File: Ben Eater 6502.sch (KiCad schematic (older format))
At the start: 8 parts, among them SW1 Reset, U1 W65C02SxP, U2 4011, U3 28C256, U4 4011, U5 W65C22SxP

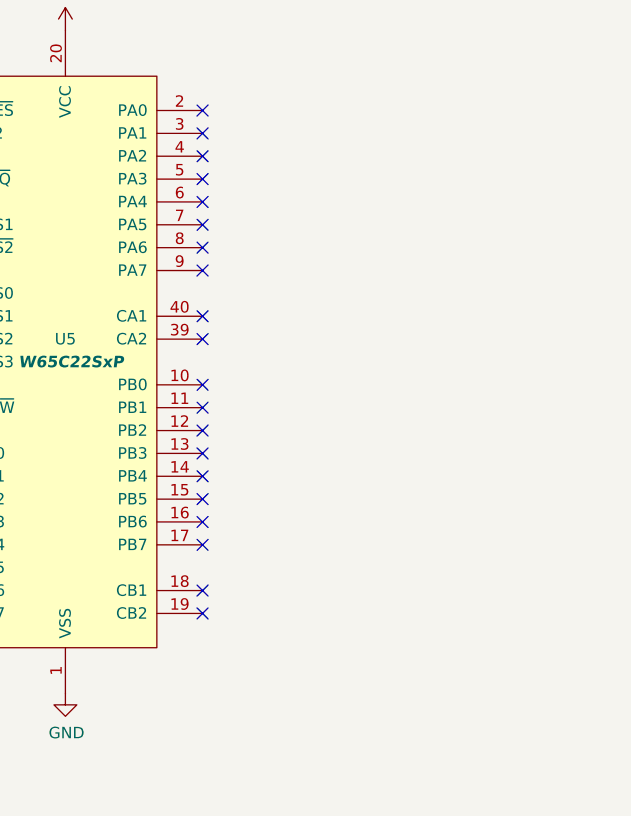
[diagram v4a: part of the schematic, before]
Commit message: Stage 3
Add display module
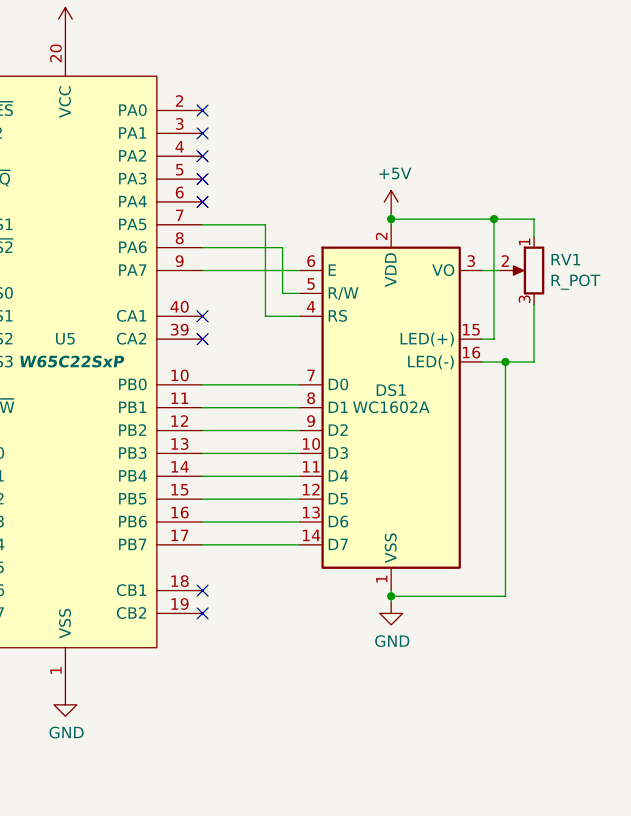
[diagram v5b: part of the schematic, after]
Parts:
- added DS1: WC1602A, Display:WC1602A, symbol Display_Character:WC1602A
- added RV1: R_POT, symbol Device:R_POT
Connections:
- net +5V: now also DS1.15 (LED(+)), DS1.2 (VDD), RV1.1
- net GND: now also DS1.1 (VSS), DS1.16 (LED(-)), RV1.3
- net at U5.10 (PB0): now also DS1.7 (D0)
- net at U5.11 (PB1): now also DS1.8 (D1)
- net at U5.12 (PB2): now also DS1.9 (D2)
- net at U5.13 (PB3): now also DS1.10 (D3)
- net at U5.14 (PB4): now also DS1.11 (D4)
- net at U5.15 (PB5): now also DS1.12 (D5)
- net at U5.16 (PB6): now also DS1.13 (D6)
- net at U5.17 (PB7): now also DS1.14 (D7)
- net at U5.7 (PA5): now also DS1.4 (RS)
- net at U5.8 (PA6): now also DS1.5 (R/W)
- net at U5.9 (PA7): now also DS1.6 (E)
- new net: DS1.3 (VO), RV1.2
- no-connect marks 26 -> 15
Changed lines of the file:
@@
 encoding utf-8
 Sheet 1 1
-Title "Ben Eater 6502 - Stage 2"
+Title "Ben Eater 6502 - Stage 3"
 Date "2021-03-22"
 Rev ""
@@
 	5025 4200 5225 4200
 NoConn ~ 5225 3000
-NoConn ~ 6425 4500
-NoConn ~ 6425 4600
 NoConn ~ 6425 4800
 NoConn ~ 6425 4900
-NoConn ~ 6425 4400
-NoConn ~ 6425 4300
-NoConn ~ 6425 4200
-NoConn ~ 6425 4100
-NoConn ~ 6425 4000
-NoConn ~ 6425 3900
 NoConn ~ 6425 3700
 NoConn ~ 6425 3600
-NoConn ~ 6425 3400
-NoConn ~ 6425 3300
-NoConn ~ 6425 3200
 NoConn ~ 6425 3100
 NoConn ~ 6425 3000
@@
 Wire Wire Line
 	1200 2275 1150 2275
+$Comp
+L Display_Character:WC1602A DS1
+U 1 1 6067F661
+P 7250 4000
+F 0 "DS1" H 7250 4075 50  0000 C CNN
+F 1 "WC1602A" H 7250 4000 50  0000 C CNN
+F 2 "Display:WC1602A" H 7250 3100 50  0001 C CIN
+F 3 "http://www.wincomlcd.com/pdf/WC1602A-SFYLYHTC06.pdf" H 7950 4000 50  0001 C CNN
+	1    7250 4000
+	1    0    0    -1
+$EndComp
+Wire Wire Line
+	6425 4600 6850 4600
+$Comp
+L power:GND #PWR08
+U 1 1 6069A086
+P 7250 4850
+F 0 "#PWR08" H 7250 4600 50  0001 C CNN
+F 1 "GND" H 7255 4677 50  0000 C CNN
+F 2 "" H 7250 4850 50  0001 C CNN
+F 3 "" H 7250 4850 50  0001 C CNN
+	1    7250 4850
+	1    0    0    -1
+$EndComp
+$Comp
+L power:+5V #PWR07
+U 1 1 6069A578
+P 7250 3150
+F 0 "#PWR07" H 7250 3000 50  0001 C CNN
+F 1 "+5V" H 7265 3323 50  0000 C CNN
+F 2 "" H 7250 3150 50  0001 C CNN
+F 3 "" H 7250 3150 50  0001 C CNN
+	1    7250 3150
+	1    0    0    -1
+$EndComp
+Wire Wire Line
+	6425 4500 6850 4500
+Wire Wire Line
+	6850 4400 6425 4400
+Wire Wire Line
+	6425 4300 6850 4300
+Wire Wire Line
+	6850 4200 6425 4200
+Wire Wire Line
+	6425 4100 6850 4100
+Wire Wire Line
+	6850 4000 6425 4000
+Wire Wire Line
+	6425 3900 6850 3900
+Wire Wire Line
+	7250 4825 7750 4825
+Wire Wire Line
+	7750 4825 7750 3800
+Wire Wire Line
+	7750 3800 7650 3800
+$Comp
+L Device:R_POT RV1
+U 1 1 606C4510
+P 7875 3400
+F 0 "RV1" H 7805 3446 50  0000 R CNN
+F 1 "R_POT" H 7805 3355 50  0000 R CNN
+F 2 "" H 7875 3400 50  0001 C CNN
+F 3 "~" H 7875 3400 50  0001 C CNN
+	1    7875 3400
+	-1   0    0    -1
+$EndComp
+Wire Wire Line
+	7650 3400 7725 3400
+Wire Wire Line
+	7875 3550 7875 3800
+Wire Wire Line
+	7875 3800 7750 3800
+Connection ~ 7750 3800
+Wire Wire Line
+	7650 3700 7700 3700
+Wire Wire Line
+	7700 3700 7700 3175
+Wire Wire Line
+	7700 3175 7875 3175
+Wire Wire Line
+	7875 3175 7875 3250
+Wire Wire Line
+	7700 3175 7250 3175
+Wire Wire Line
+	7250 3175 7250 3200
+Connection ~ 7700 3175
+Wire Wire Line
+	7250 3150 7250 3175
+Connection ~ 7250 3175
+Wire Wire Line
+	7250 4850 7250 4825
+Connection ~ 7250 4825
+Wire Wire Line
+	7250 4825 7250 4800
+Wire Wire Line
+	6425 3400 6850 3400
+Wire Wire Line
+	6425 3300 6775 3300
+Wire Wire Line
+	6775 3300 6775 3500
+Wire Wire Line
+	6775 3500 6850 3500
+Wire Wire Line
+	6425 3200 6700 3200
+Wire Wire Line
+	6700 3200 6700 3600
+Wire Wire Line
+	6700 3600 6850 3600
 Wire Bus Line
 	4925 2025 4925 3700

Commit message: Stage 4
Add RAM
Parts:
- added unit 3 of U2
- added U4: AS6C62256A, Package_DIP:DIP-28_W15.24mm, symbol Memory_RAM:KM62256CLP
- renumbered U4 to U2
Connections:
- net +5V: now also U4.28 (VCC)
- net CLOCK: now also U2.9
- net GND: now also U4.14 (GND)
- net a0: now also U4.10 (A0)
- net a1: now also U4.9 (A1)
- net a10: now also U4.21 (A10)
- net a11: now also U4.23 (A11)
- net a12: now also U4.2 (A12)
- net a13: now also U4.26 (A13)
- net a14: now also U2.6, U4.1 (A14), U4.22 (~OE); no longer U2.2
- net a2: now also U4.8 (A2)
- net a3: now also U4.7 (A3)
- net a4: now also U4.6 (A4)
- net a5: now also U4.5 (A5)
- net a6: now also U4.4 (A6)
- net a7: now also U4.3 (A7)
- net a8: now also U4.25 (A8)
- net a9: now also U4.24 (A9)
- net d0: now also U4.11 (Q0)
- net d1: now also U4.12 (Q1)
- net d2: now also U4.13 (Q2)
- net d3: now also U4.15 (Q3)
- net d4: now also U4.16 (Q4)
- net d5: now also U4.17 (Q5)
- net d6: now also U4.18 (Q6)
- net d7: now also U4.19 (Q7)
- net ~a15: no longer U2.1, U2.3, U3.20 (~CS)
- net at U1.34 (R/~W), U5.22 (R/~W): now also U4.27 (~WE)
- net at U5.23 (~CS2): now also U2.4; no longer U2.3
- new net: U2.3, U2.5, U2.8, U3.20 (~CS)
- new net: U2.10, U4.20 (~CS)
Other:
- moved on the sheet: DS1, RV1, U2A, U3, U5

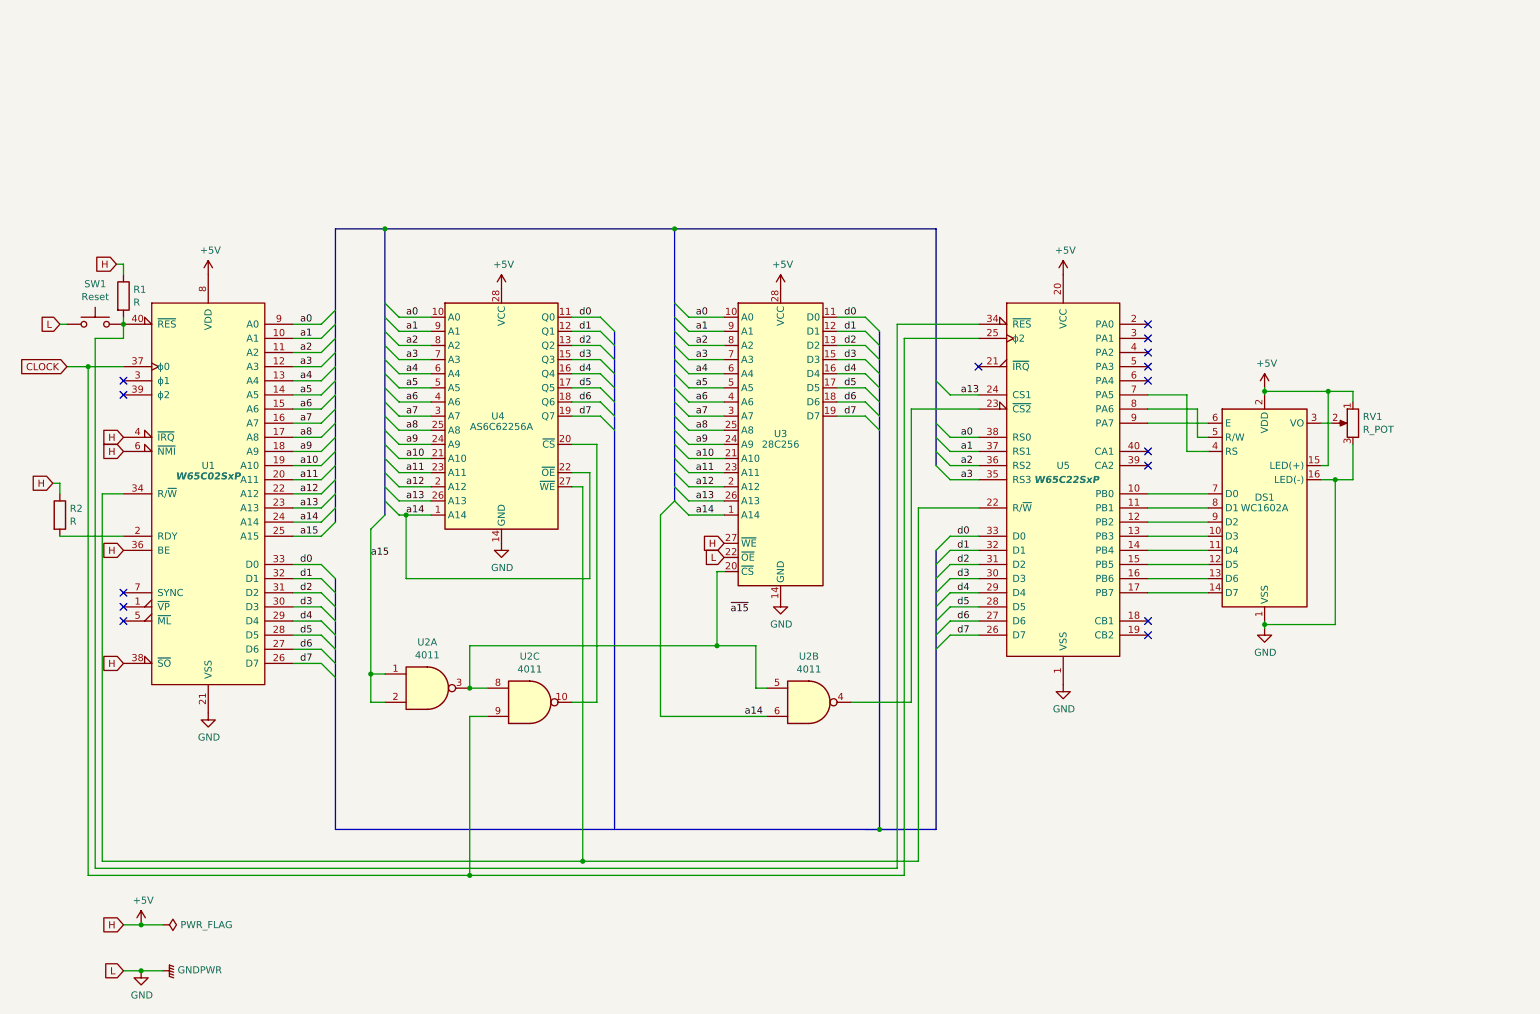
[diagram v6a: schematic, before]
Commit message: Stage 5
Add NMI & IRQ push buttons with pull-up resisitors
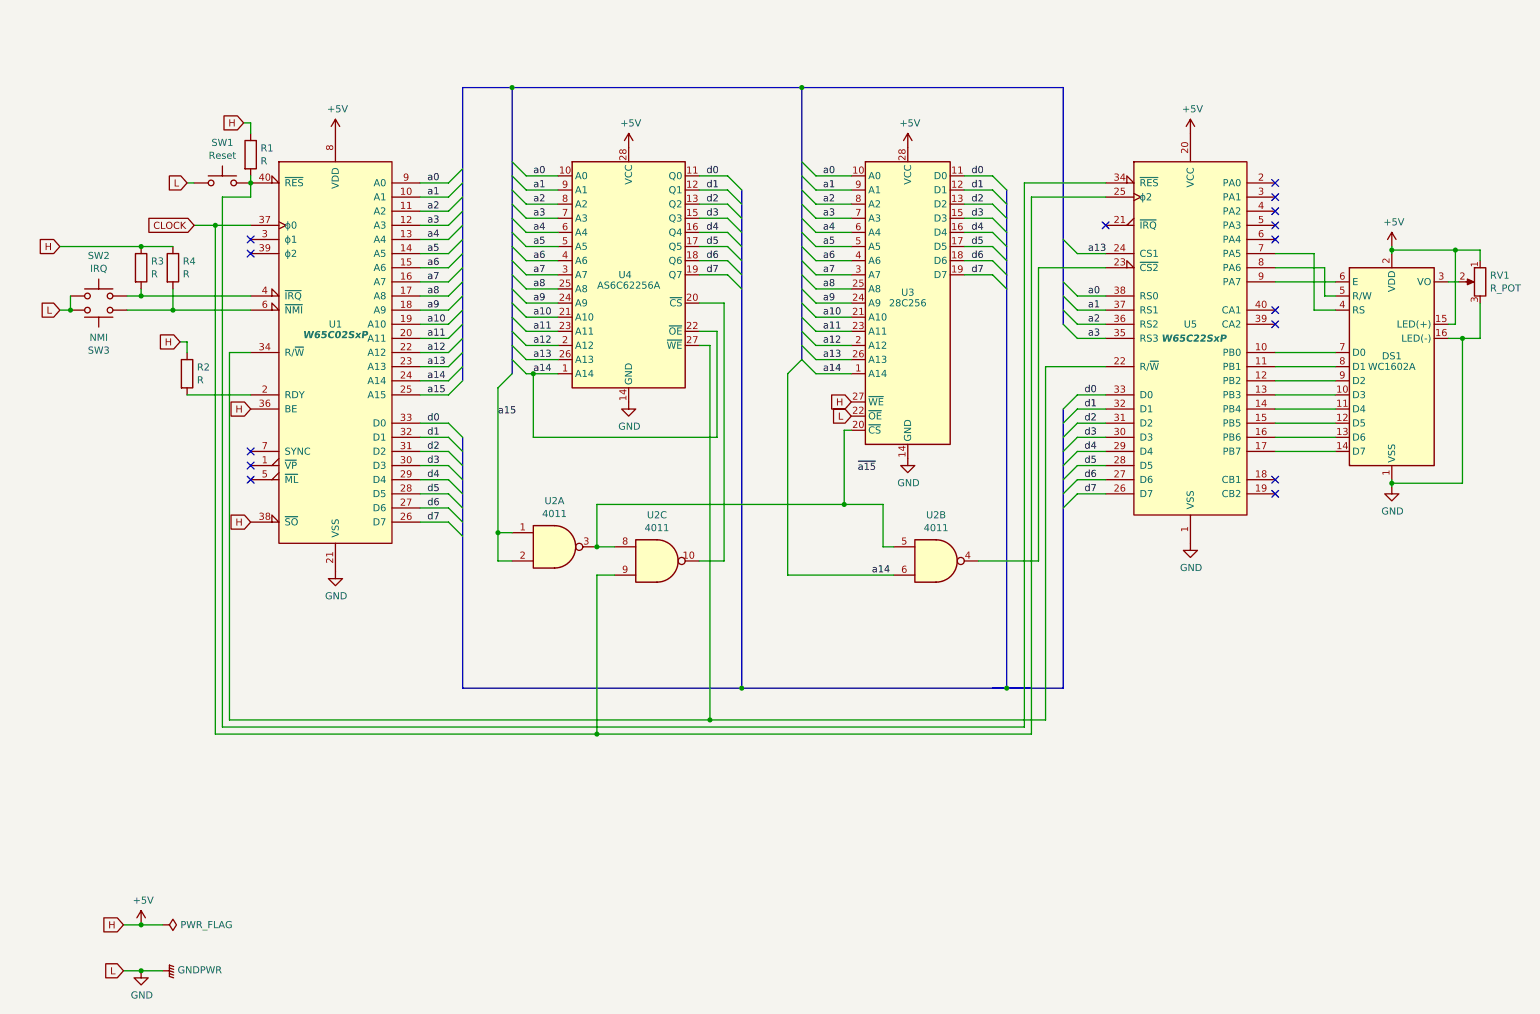
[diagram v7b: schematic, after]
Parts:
- added R3, R4: R, symbol Device:R
- added SW2: IRQ, symbol Switch:SW_Push
- added SW3: NMI, symbol Switch:SW_Push
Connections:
- net +5V: now also R3.1, R4.1; no longer U1.4 (~IRQ), U1.6 (~NMI)
- net GND: now also SW2.1, SW3.2
- new net: R3.2, SW2.2, U1.4 (~IRQ)
- new net: R4.2, SW3.1, U1.6 (~NMI)
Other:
- moved on the sheet: DS1, R1, R2, RV1, SW1, U1, U2A, U2B, U2C, U3, U4, U5

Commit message: Stage 6
Connect IRQ line from 6552 to 6502.

Move LCD data pins from 6552 port B to port A, and the control pins from
PA5-7 to PB0-2, to allow us to connect the keyboard clock pin to PB6.

Add keyboard connector. Clock connects via an inverter to CB1, data
connects directly to CB2.

The unused fourth set of inputs on the quad 2-nand gate is used as the
inverter.
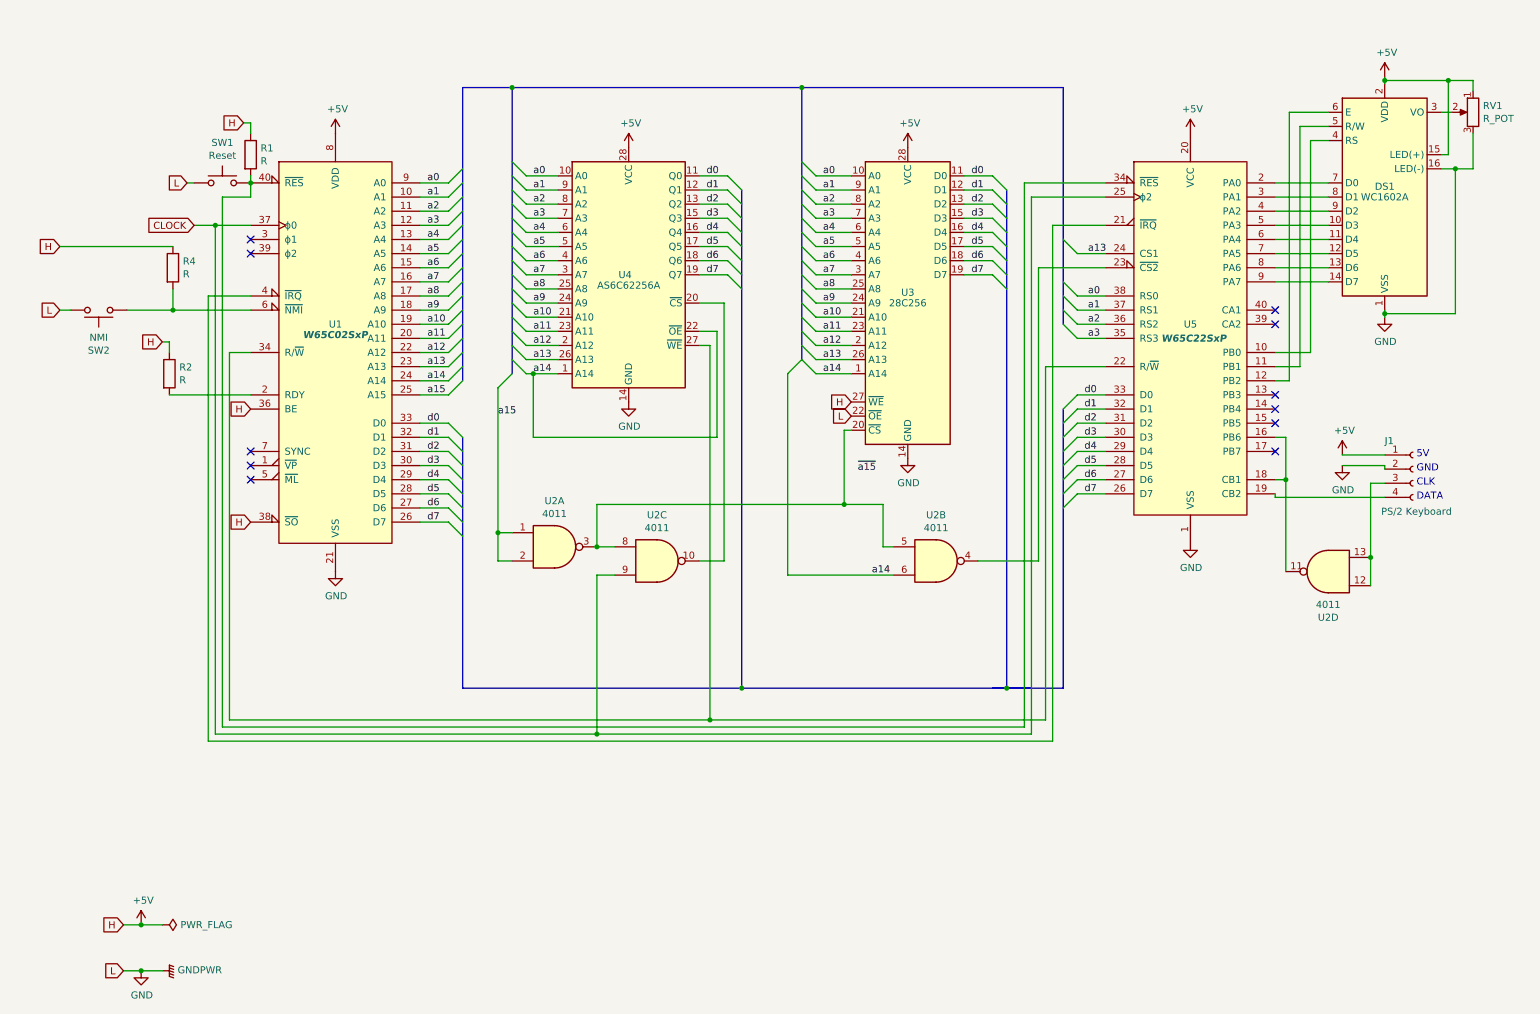
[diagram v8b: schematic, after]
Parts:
- removed R3: R, symbol Device:R
- removed SW2: IRQ, symbol Switch:SW_Push
- added J1: PS/2 Keyboard, symbol Connector:Conn_01x04_Female
- added unit 4 of U2
- renumbered SW3 to SW2
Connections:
- net +5V: now also J1.1 (Pin_1)
- net GND: now also J1.2 (Pin_2)
- net at U1.4 (~IRQ): now also U5.21 (~IRQ)
- net at U5.10 (PB0): now also DS1.4 (RS); no longer DS1.7 (D0)
- net at U5.11 (PB1): now also DS1.5 (R/W); no longer DS1.8 (D1)
- net at U5.12 (PB2): now also DS1.6 (E); no longer DS1.9 (D2)
- net at U5.13 (PB3): no longer DS1.10 (D3)
- net at U5.14 (PB4): no longer DS1.11 (D4)
- net at U5.15 (PB5): no longer DS1.12 (D5)
- net at U5.16 (PB6): now also U5.18 (CB1), U2.11; no longer DS1.13 (D6)
- net at U5.17 (PB7): no longer DS1.14 (D7)
- net at U5.19 (CB2): now also J1.4 (Pin_4)
- net at U5.2 (PA0): now also DS1.7 (D0)
- net at U5.3 (PA1): now also DS1.8 (D1)
- net at U5.4 (PA2): now also DS1.9 (D2)
- net at U5.5 (PA3): now also DS1.10 (D3)
- net at U5.6 (PA4): now also DS1.11 (D4)
- net at U5.7 (PA5): now also DS1.12 (D5); no longer DS1.4 (RS)
- net at U5.8 (PA6): now also DS1.13 (D6); no longer DS1.5 (R/W)
- net at U5.9 (PA7): now also DS1.14 (D7); no longer DS1.6 (E)
- new net: J1.3 (Pin_3), U2.12, U2.13
- no-connect marks 15 -> 11
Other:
- note added: "5V"
- note added: "CLK"
- note added: "DATA"
- note added: "GND"
- moved on the sheet: DS1, R2, RV1
